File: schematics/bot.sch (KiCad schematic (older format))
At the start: 21 parts

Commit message: Remap Kicad symbols
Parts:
- J? (x2): symbol Conn_01x16_Male -> bot-rescue:Conn_01x16_Male
- R? (x14): symbol R -> bot-rescue:R
- U? (x4): symbol 74HC595 -> bot-rescue:74HC595
- U?: symbol STM32F103C8Tx -> MCU_ST_STM32F1:STM32F103C8Tx
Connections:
- wire segments 129 -> 138
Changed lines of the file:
@@
-EESchema Schematic File Version 2
-LIBS:power
-LIBS:device
-LIBS:switches
-LIBS:relays
-LIBS:motors
-LIBS:transistors
-LIBS:conn
-LIBS:linear
-LIBS:regul
-LIBS:74xx
-LIBS:cmos4000
-LIBS:adc-dac
-LIBS:memory
-LIBS:microcontrollers
-LIBS:xilinx
-LIBS:dsp
-LIBS:microchip
-LIBS:analog_switches
-LIBS:motorola
-LIBS:texas
-LIBS:intel
-LIBS:audio
-LIBS:interface
-LIBS:digital-audio
-LIBS:philips
-LIBS:display
-LIBS:cypress
-LIBS:siliconi
-LIBS:opto
-LIBS:atmel
-LIBS:contrib
-LIBS:valves
-LIBS:MCU_ST_STM32F1
+EESchema Schematic File Version 4
 LIBS:bot-cache
-EELAYER 25 0
+EELAYER 26 0
 EELAYER END
 $Descr A4 11693 8268
@@
 $EndDescr
 $Comp
-L 74HC595 U?
+L bot-rescue:74HC595 U?
 U 1 1 5B12EF0E
 P 3900 1800
@@
 $EndComp
 $Comp
-L 74HC595 U?
+L bot-rescue:74HC595 U?
 U 1 1 5B12EFD5
 P 3900 3250
@@
 	4600 2550 4600 2800
 $Comp
-L +3.3V #PWR?
+L power:+3.3V #PWR?
 U 1 1 5B12F1E6
 P 4600 1650
@@
 $EndComp
 $Comp
-L +3.3V #PWR?
+L power:+3.3V #PWR?
 U 1 1 5B12F222
 P 4600 3100
@@
 $EndComp
 Wire Wire Line
-	4600 1550 6950 1550
-Wire Wire Line
-	4850 1550 4850 6250
+	4600 1550 4850 1550
+Wire Wire Line
+	4850 1550 4850 3000
 Wire Wire Line
 	4850 3000 4600 3000
 Wire Wire Line
-	4600 1850 7000 1850
-Wire Wire Line
-	5000 1850 5000 6550
+	4600 1850 5000 1850
+Wire Wire Line
+	5000 1850 5000 3300
 Wire Wire Line
 	5000 3300 4600 3300
 Wire Wire Line
-	4600 1950 6850 1950
-Wire Wire Line
-	5150 1950 5150 6650
+	4600 1950 5150 1950
+Wire Wire Line
+	5150 1950 5150 3400
 Wire Wire Line
 	5150 3400 4600 3400
 $Comp
-L Conn_01x16_Male J?
+L bot-rescue:Conn_01x16_Male J?
 U 1 1 5B12FAF9
 P 1850 1950
@@
 $EndComp
 $Comp
-L R R?
+L bot-rescue:R R?
 U 1 1 5B12FE45
 P 2200 1150
@@
 $EndComp
 $Comp
-L R R?
+L bot-rescue:R R?
 U 1 1 5B12FF9A
 P 2200 2450
@@
 $EndComp
 $Comp
-L R R?
+L bot-rescue:R R?
 U 1 1 5B130113
 P 2200 2150
@@
 $EndComp
 $Comp
-L R R?
+L bot-rescue:R R?
 U 1 1 5B130193
 P 2200 1750
@@
 $EndComp
 $Comp
-L R R?
+L bot-rescue:R R?
 U 1 1 5B130246
 P 2200 1650
@@
 $EndComp
 $Comp
-L R R?
+L bot-rescue:R R?
 U 1 1 5B130303
 P 2200 1450
@@
 $EndComp
 $Comp
-L R R?
+L bot-rescue:R R?
 U 1 1 5B13035F
 P 2200 1250
@@
 	2600 3500 3200 3500
 $Comp
-L 74HC595 U?
+L bot-rescue:74HC595 U?
 U 1 1 5B132614
 P 3900 5050
@@
 $EndComp
 $Comp
-L 74HC595 U?
+L bot-rescue:74HC595 U?
 U 1 1 5B13261A
 P 3900 6500
@@
 	4600 5800 4600 6050
 $Comp
-L +3.3V #PWR?
+L power:+3.3V #PWR?
 U 1 1 5B132623
 P 4600 4900
@@
 $EndComp
 $Comp
-L +3.3V #PWR?
+L power:+3.3V #PWR?
 U 1 1 5B132629
 P 4600 6350
@@
 	5150 6650 4600 6650
 $Comp
-L Conn_01x16_Male J?
+L bot-rescue:Conn_01x16_Male J?
 U 1 1 5B132638
 P 1850 5200
@@
 $EndComp
 $Comp
-L R R?
+L bot-rescue:R R?
 U 1 1 5B13263E
 P 2200 4400
@@
 $EndComp
 $Comp
-L R R?
+L bot-rescue:R R?
 U 1 1 5B132644
 P 2200 5700
@@
 $EndComp
 $Comp
-L R R?
+L bot-rescue:R R?
 U 1 1 5B13264A
 P 2200 5400
@@
 $EndComp
 $Comp
-L R R?
+L bot-rescue:R R?
 U 1 1 5B132650
 P 2200 5000
@@
 $EndComp
 $Comp
-L R R?
+L bot-rescue:R R?
 U 1 1 5B132656
 P 2200 4900
@@
 $EndComp
 $Comp
-L R R?
+L bot-rescue:R R?
 U 1 1 5B13265C
 P 2200 4700
@@
 $EndComp
 $Comp
-L R R?
+L bot-rescue:R R?
 U 1 1 5B132662
 P 2200 4500
@@
 Connection ~ 5150 3400
 $Comp
-L STM32F103C8Tx U?
+L MCU_ST_STM32F1:STM32F103C8Tx U?
 U 1 1 5B1300F7
 P 7800 3350
@@
 $EndComp
 $Comp
-L +3.3V #PWR?
+L power:+3.3V #PWR?
 U 1 1 5B130C16
 P 7700 1850
@@
 $EndComp
 $Comp
-L GND #PWR?
+L power:GND #PWR?
 U 1 1 5B13112B
 P 7600 4850
@@
 	7000 3450 7000 1850
 Connection ~ 5000 1850
+Wire Wire Line
+	4850 4800 4850 6250
+Wire Wire Line
+	4850 3000 4850 4800
+Wire Wire Line
+	5000 5100 5000 6550
+Wire Wire Line
+	5000 3300 5000 5100
+Wire Wire Line
+	5150 5200 5150 6650
+Wire Wire Line
+	5150 3400 5150 5200
+Wire Wire Line
+	5150 1950 6850 1950
+Wire Wire Line
+	4850 1550 6950 1550
+Wire Wire Line
+	5000 1850 7000 1850
 $EndSCHEMATC

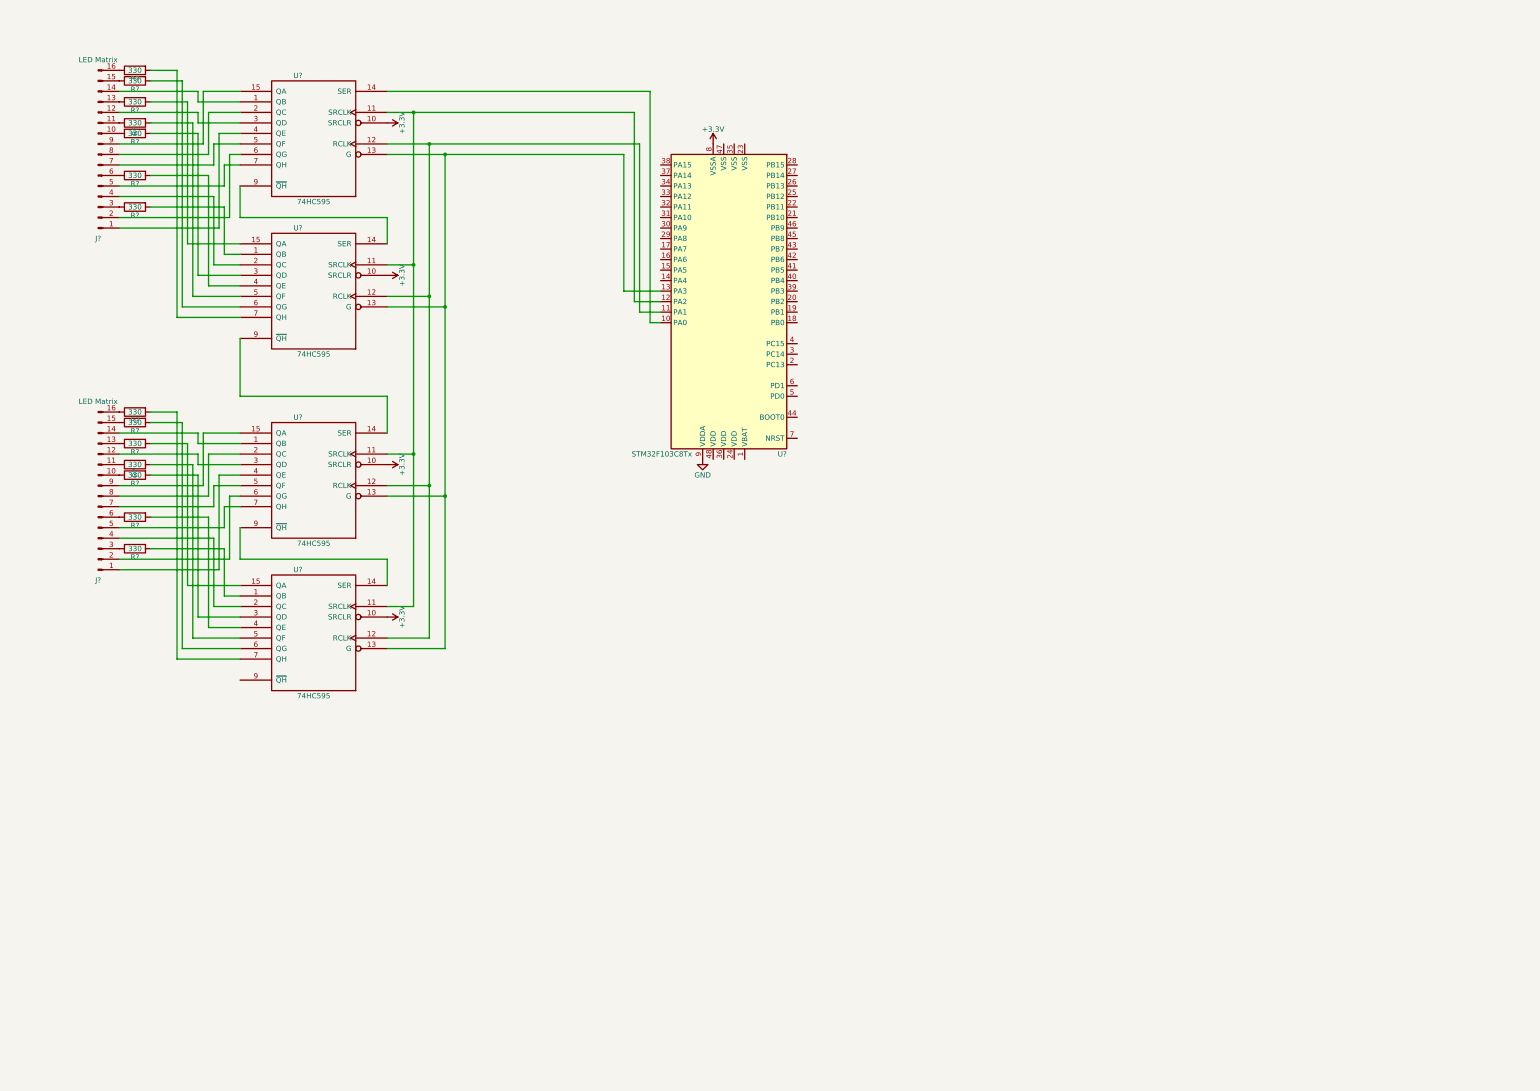
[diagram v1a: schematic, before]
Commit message: Add servos control schematic
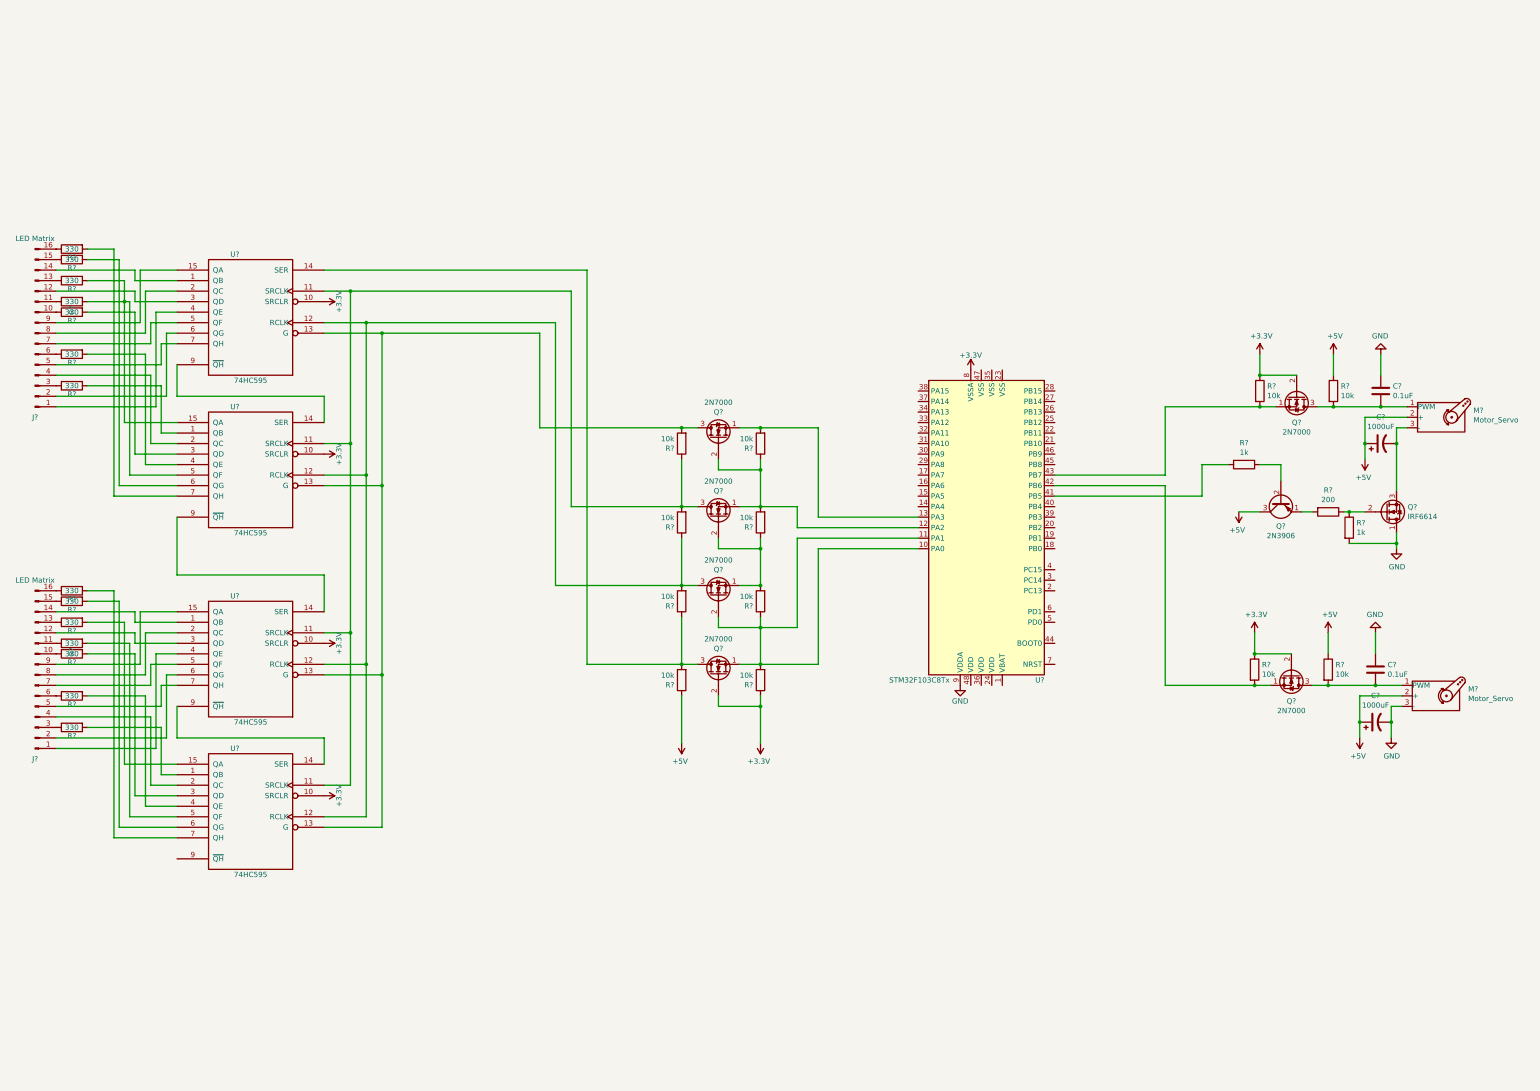
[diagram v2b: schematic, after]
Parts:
- added C? (x2): 1000uF, symbol Device:CP1
- added C? (x2): 0.1uF, symbol Device:C
- added M? (x2): Motor_Servo, symbol Motor:Motor_Servo
- added Q? (x6): 2N7000, Package_TO_SOT_THT:TO-92_Inline, symbol Transistor_FET:2N7000
- added Q?: IRF6614, Package_DirectFET:DirectFET_ST, symbol Transistor_FET:IRF6614
- added Q?: 2N3906, Package_TO_SOT_THT:TO-92_Inline, symbol Transistor_BJT:2N3906
- added R? (x12): 10k, symbol bot-rescue:R
- added R?: 200, symbol bot-rescue:R
- added R? (x2): 1k, symbol bot-rescue:R
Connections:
- net +3V3: now also Q?.2 (G), Q?.2 (G), Q?.2 (G), R?.1, R?.1, R?.1
- net GND: now also C?.1, C?.1, C?.2, M?.3 (-), Q?.1 (D), R?.2
- net at U?.11 (SRCLK), U?.11 (SRCLK), U?.11 (SRCLK)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: now also Q?.3 (D), R?.1, R?.2; no longer U?.12 (PA2)
- net at U?.12 (RCLK), U?.12 (RCLK), U?.12 (RCLK)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: now also Q?.3 (D), R?.1, R?.2; no longer U?.11 (PA1)
- net at U?.13 (G), U?.13 (G), U?.13 (G)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: now also Q?.3 (D), R?.2; no longer U?.13 (PA3)
- net at U?.14 (SER): now also Q?.3 (D), R?.1, R?.2; no longer U?.10 (PA0)
- net at R?.2, U?.15 (QA): now also R?.2, U?.5 (QF)
- net at U?.41 (PB5): now also R?.2
- net at U?.42 (PB6): now also Q?.1 (S), R?.2
- net at U?.43 (PB7): now also Q?.1 (S), R?.2
- new net: Q?.1 (S), Q?.2 (G), R?.1, R?.2, U?.10 (PA0), U?.11 (PA1)
- new net: Q?.1 (S), Q?.2 (G), R?.1, R?.2, U?.12 (PA2)
- new net: Q?.1 (S), R?.2, U?.13 (PA3)
- new net: C?.2, M?.1 (PWM), Q?.3 (D), R?.2 (x2)
- new net: C?.2, M?.3 (-), Q?.3 (S)
- new net: Q?.2 (G), R?.1, R?.1
- new net: Q?.1 (E), R?.2
- new net: Q?.2 (B), R?.1
- new net: Q?.1 (S), Q?.2 (G), R?.1, R?.2
- new net +5V: C?.1, C?.1, M?.2 (+), M?.2 (+), Q?.3 (C), R?.1, R?.1, R?.1
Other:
- moved on the sheet: J?, R?, U?

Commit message: uC support circuitry schematics
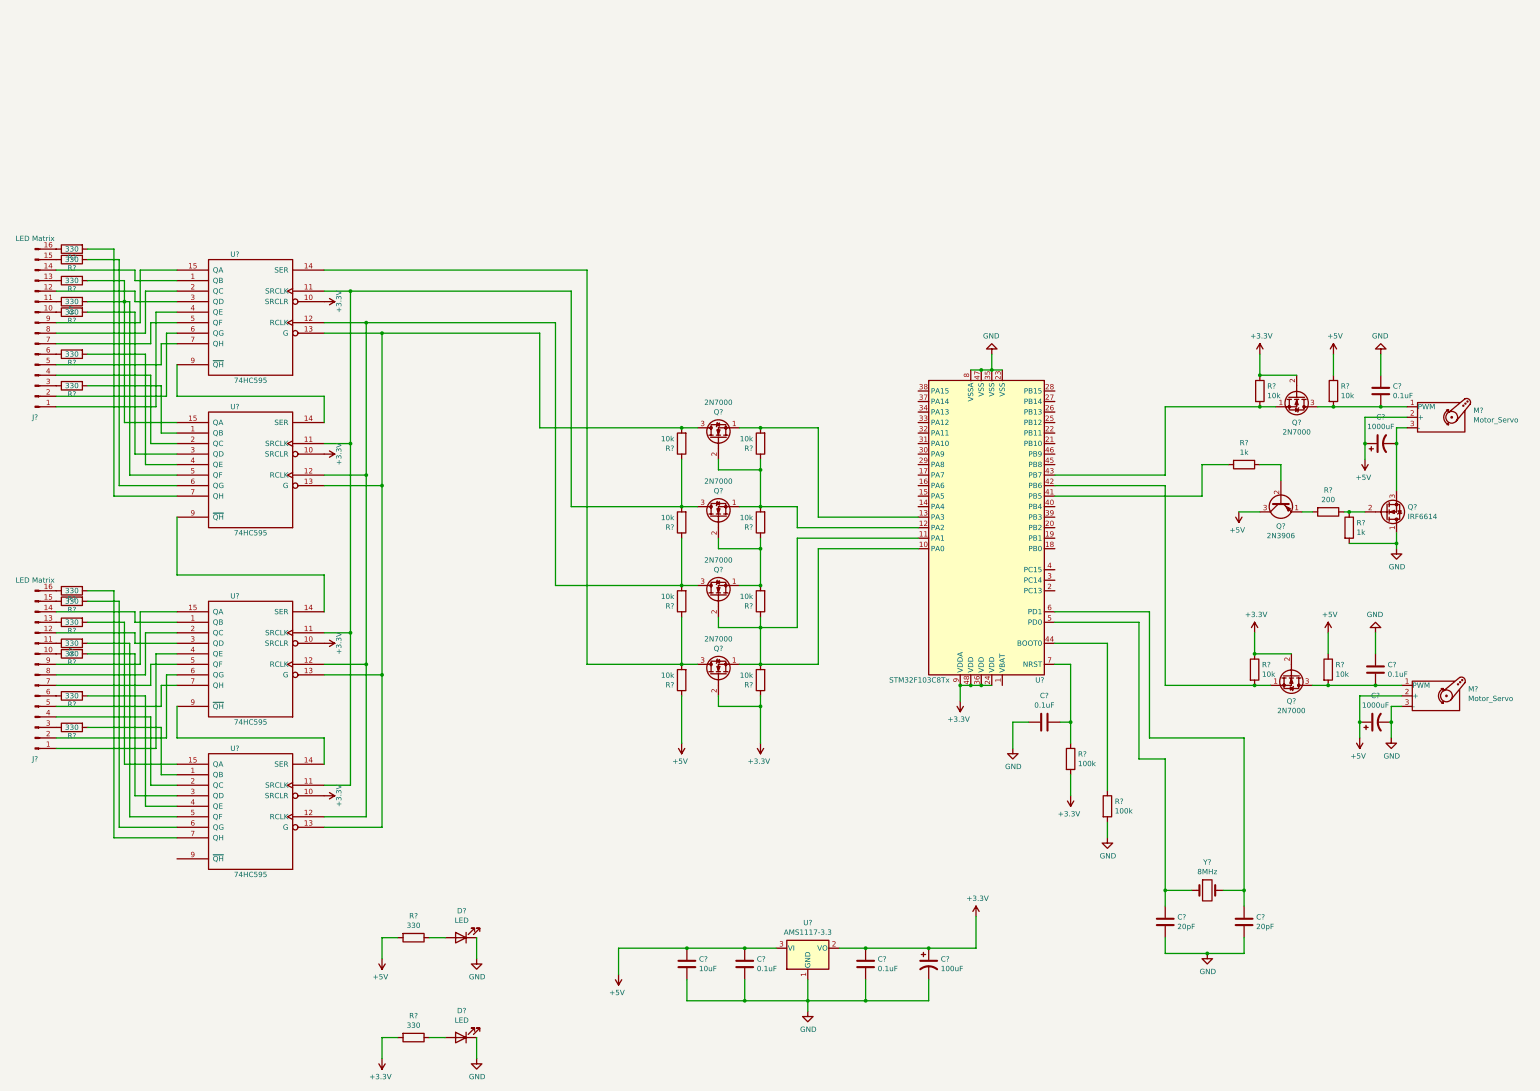
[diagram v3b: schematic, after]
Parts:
- added C? (x2): 20pF, symbol Device:C
- added C? (x3): 0.1uF, symbol Device:C
- added C?: 10uF, symbol Device:C
- added C?: 100uF, symbol Device:CP1
- added D? (x2): LED, symbol Device:LED
- added R? (x2): 100k, symbol bot-rescue:R
- added R? (x2): 330, symbol bot-rescue:R
- added U?: AMS1117-3.3, Package_TO_SOT_SMD:SOT-223-3_TabPin2, symbol Regulator_Linear:AMS1117-3.3
- added Y?: 8MHz, symbol Device:Crystal
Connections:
- net +3V3: now also U?.24 (VDD), U?.36 (VDD), U?.48 (VDD), U?.9 (VDDA), C?.1, C?.1, R?.2, R?.2, U?.2 (VO); no longer U?.8 (VSSA)
- net +5V: now also C?.1, C?.1, R?.2, U?.3 (VI)
- net GND: now also U?.23 (VSS), U?.35 (VSS), U?.47 (VSS), U?.8 (VSSA), C?.1, C?.2, C?.2, C?.2, C?.2, C?.2, C?.2, D?.1 (K), D?.1 (K), R?.2, U?.1 (GND); no longer U?.9 (VDDA)
- net at U?.44 (BOOT0): now also R?.1
- net at U?.5 (PD0): now also C?.1, Y?.1
- net at U?.6 (PD1): now also C?.1, Y?.2
- net at U?.7 (NRST): now also C?.2, R?.1
- new net: D?.2 (A), R?.1 (x2)

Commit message: UART-USB schematic
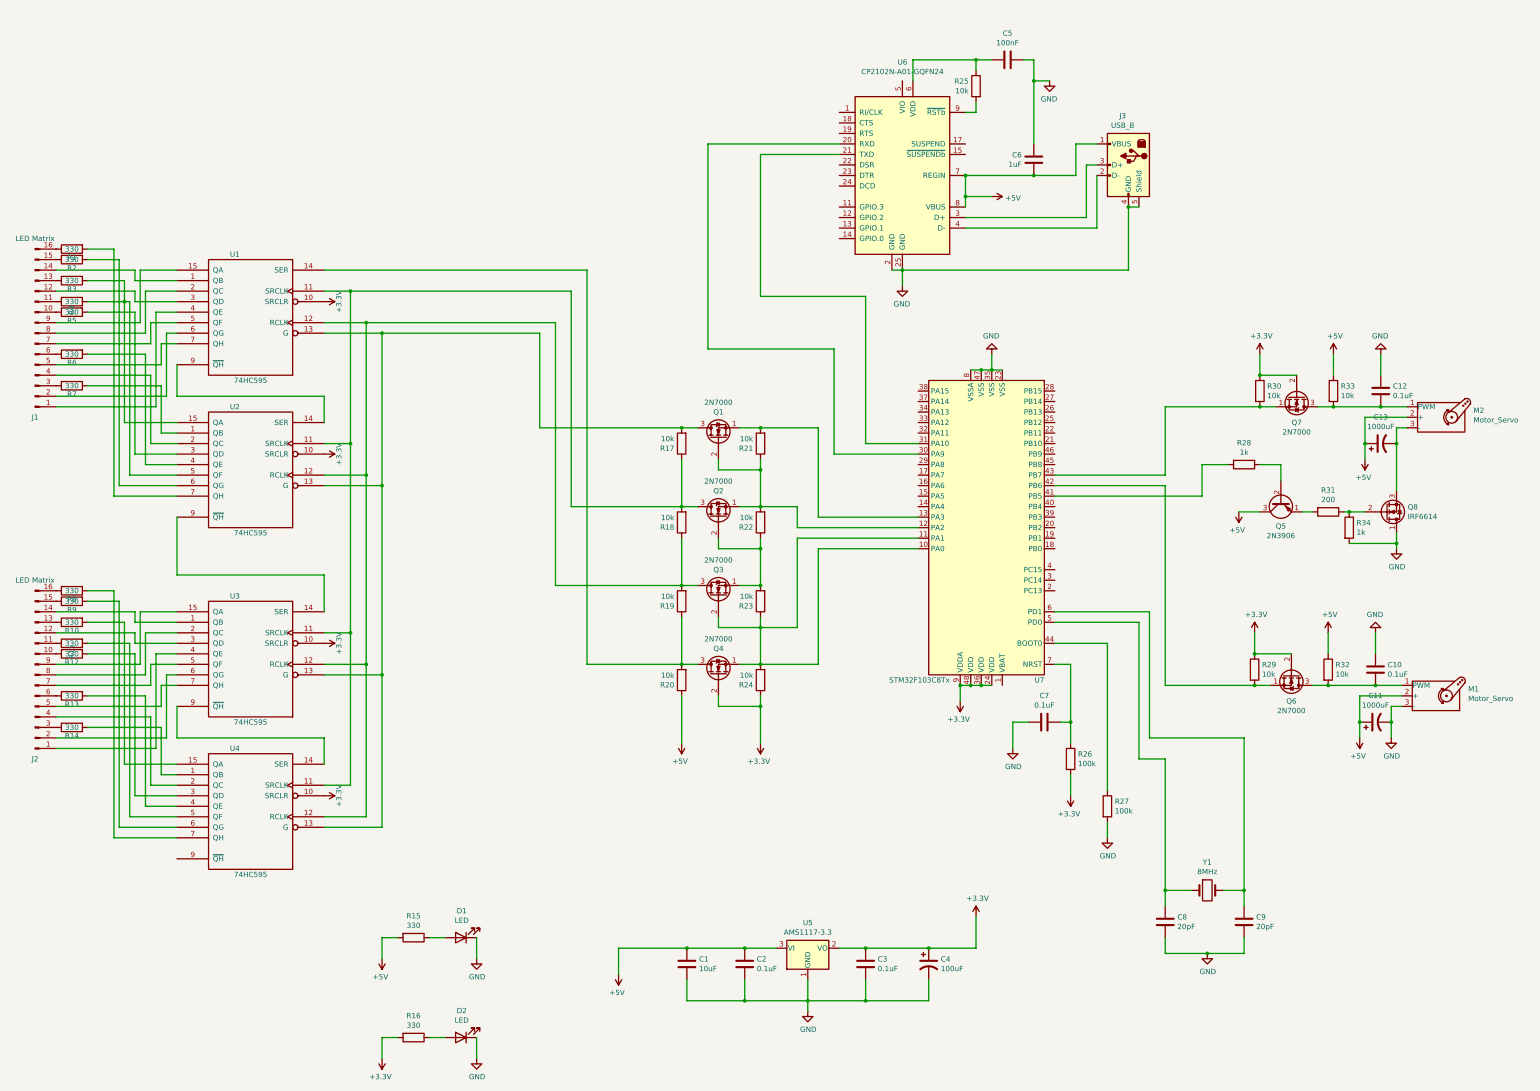
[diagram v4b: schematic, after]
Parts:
- added C5: 100nF, symbol Device:C
- added C6: 1uF, symbol Device:C
- added J3: USB_B, symbol Connector:USB_B
- added R25: 10k, symbol bot-rescue:R
- added U6: CP2102N-A01-GQFN24, Package_DFN_QFN:QFN-24-1EP_4x4mm_P0.5mm_EP2.6x2.6mm, symbol Interface_USB:CP2102N-A01-GQFN24
- gave numbers to parts that had none: 65
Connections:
- net +5V: now also C6.2, J3.1 (VBUS), U6.7 (REGIN), U6.8 (VBUS)
- net GND: now also C5.2, C6.1, J3.4 (GND), J3.5 (Shield), U6.2 (GND), U6.25 (GND)
- net at U7.30 (PA9): now also U6.20 (RXD)
- net at U7.31 (PA10): now also U6.21 (TXD)
- new net: J3.3 (D+), U6.3 (D+)
- new net: J3.2 (D-), U6.4 (D-)
- new net: C5.1, R25.1, U6.6 (VDD)
- new net: R25.2, U6.9 (~RSTb)
